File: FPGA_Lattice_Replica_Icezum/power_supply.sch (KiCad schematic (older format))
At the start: 53 parts, among them J18 Power_Jack, Q1 DMP3017, Q2 DMP3017, Q3 DMP2035U-7, Q4 Mosfet_P_DFN-6, Q5 PMBT3906, SW3 SPDT_Switch, SW4 Switch, U10 AP7361, U11 TLV711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

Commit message: se finalizo asignación de footprint de acuerdo al modelo original de la icezum alhambra
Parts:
- C59, C61: footprint (none) -> footprints:C_0603
- C63, C68: footprint (none) -> footprints:C_0402
- J18: footprint (none) -> footprints:JACK_2.1
- L4: footprint (none) -> footprints:L_0603
- L5: footprint (none) -> footprints:L_4040
- Q1, Q2, Q4: footprint (none) -> footprints:DFN-2523-6
- Q3, U13: footprint (none) -> footprints:SOT-23
- Q5: footprint Package_TO_SOT_SMD:SOT-363_SC-70-6 -> footprints:SOT-23
- R24, R25, R26, R27, R28, R29, R30, R33, R34, R35, R36, R37, R38, R39: footprint (none) -> footprints:R_0402
- SW3: footprint (none) -> footprints:slide-sw-spdt-right-angle
- SW4: footprint (none) -> footprints:SW_vert_tht_7.5x6x6.5
- TP1, TP2, TP3, TP4, TP5, TP6, TP7: footprint (none) -> footprints:Via_Test_point
- U10: footprint (none) -> footprints:DFN-3030-8
- U11: footprint (none) -> footprints:WSON-6
- U12: footprint (none) -> footprints:QFN16
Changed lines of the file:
@@
 F 0 "J18" H 3107 3925 50  0000 C CNN
 F 1 "Power_Jack" H 3107 3834 50  0000 C CNN
-F 2 "" H 3100 3560 50  0001 C CNN
+F 2 "footprints:JACK_2.1" H 3100 3560 50  0001 C CNN
 F 3 "~" H 3100 3560 50  0001 C CNN
 	1    3050 3600
@@
 F 0 "Q1" V 3702 3850 60  0000 C CNN
 F 1 "DMP3017" V 3808 3850 60  0000 C CNN
-F 2 "" H 4540 3830 60  0001 C CNN
+F 2 "footprints:DFN-2523-6" H 4540 3830 60  0001 C CNN
 F 3 "" H 4540 3830 60  0000 C CNN
 	1    4100 3500
@@
 F 0 "Q2" V 6102 3850 60  0000 C CNN
 F 1 "DMP3017" V 6208 3850 60  0000 C CNN
-F 2 "" H 6940 3830 60  0001 C CNN
+F 2 "footprints:DFN-2523-6" H 6940 3830 60  0001 C CNN
 F 3 "" H 6940 3830 60  0000 C CNN
 	1    6500 3500
@@
 F 0 "Q5" V 7385 4350 50  0000 C CNN
 F 1 "PMBT3906" V 7476 4350 50  0000 C CNN
-F 2 "Package_TO_SOT_SMD:SOT-363_SC-70-6" H 7350 4450 50  0001 C CNN
+F 2 "footprints:SOT-23" H 7350 4450 50  0001 C CNN
 F 3 "https://assets.nexperia.com/documents/data-sheet/PMBT3906YS.pdf" H 7150 4350 50  0001 C CNN
 	1    7150 4350
@@
 F 0 "Q3" V 7502 3975 60  0000 C CNN
 F 1 "DMP2035U-7" V 7608 3975 60  0000 C CNN
-F 2 "" H 8350 3950 60  0001 C CNN
+F 2 "footprints:SOT-23" H 8350 3950 60  0001 C CNN
 F 3 "" H 8350 3950 60  0000 C CNN
 	1    8350 3950
@@
 F 0 "C61" V 5302 3950 50  0000 C CNN
 F 1 "10 nF" V 5211 3950 50  0000 C CNN
-F 2 "" H 5088 3800 50  0001 C CNN
+F 2 "footprints:C_0603" H 5088 3800 50  0001 C CNN
 F 3 "~" H 5050 3950 50  0001 C CNN
 F 4 "X7R" V 5050 3950 50  0001 C CNN "Clase"
@@
 F 0 "R25" H 4620 4296 50  0000 L CNN
 F 1 "10K±5% 0.063 W" V 4450 3900 50  0000 L CNN
-F 2 "" V 4480 4250 50  0001 C CNN
+F 2 "footprints:R_0402" V 4480 4250 50  0001 C CNN
 F 3 "~" H 4550 4250 50  0001 C CNN
 	1    4550 4250
@@
 F 0 "R26" H 5420 4296 50  0000 L CNN
 F 1 "100K±5% 0.063 W" V 5250 3800 50  0000 L CNN
-F 2 "" V 5280 4250 50  0001 C CNN
+F 2 "footprints:R_0402" V 5280 4250 50  0001 C CNN
 F 3 "~" H 5350 4250 50  0001 C CNN
 	1    5350 4250
@@
 F 0 "R27" H 6120 4296 50  0000 L CNN
 F 1 "10K±5% 0.063 W" V 5950 3800 50  0000 L CNN
-F 2 "" V 5980 4250 50  0001 C CNN
+F 2 "footprints:R_0402" V 5980 4250 50  0001 C CNN
 F 3 "~" H 6050 4250 50  0001 C CNN
 	1    6050 4250
@@
 F 0 "R29" H 8270 4646 50  0000 L CNN
 F 1 "100K±5% 0.063 W" V 8100 4000 50  0000 L CNN
-F 2 "" V 8130 4600 50  0001 C CNN
+F 2 "footprints:R_0402" V 8130 4600 50  0001 C CNN
 F 3 "~" H 8200 4600 50  0001 C CNN
 	1    8200 4600
@@
 F 0 "R28" V 7593 4450 50  0000 C CNN
 F 1 "10K±5% 0.063 W" V 7684 4450 50  0000 C CNN
-F 2 "" V 7730 4450 50  0001 C CNN
+F 2 "footprints:R_0402" V 7730 4450 50  0001 C CNN
 F 3 "~" H 7800 4450 50  0001 C CNN
 	1    7800 4450
@@
 F 0 "R38" V 7450 3500 50  0000 C CNN
 F 1 "10K±5% 0.063 W" V 7250 3450 50  0000 C CNN
-F 2 "" V 7280 3500 50  0001 C CNN
+F 2 "footprints:R_0402" V 7280 3500 50  0001 C CNN
 F 3 "~" H 7350 3500 50  0001 C CNN
 	1    7350 3500
@@
 F 0 "R39" H 7870 3846 50  0000 L CNN
 F 1 "1K±5% 0.063 W" V 7700 3450 50  0000 L CNN
-F 2 "" V 7730 3800 50  0001 C CNN
+F 2 "footprints:R_0402" V 7730 3800 50  0001 C CNN
 F 3 "~" H 7800 3800 50  0001 C CNN
 	1    7800 3800
@@
 F 0 "TP6" H 6778 3442 60  0000 L CNN
 F 1 "TestPoint_Small" H 6700 3250 60  0001 C CNN
-F 2 "" H 6700 3350 60  0001 C CNN
+F 2 "footprints:Via_Test_point" H 6700 3350 60  0001 C CNN
 F 3 "" H 6700 3350 60  0000 C CNN
 	1    6700 3350
@@
 F 0 "SW3" H 7325 5441 47  0000 C CNN
 F 1 "SPDT_Switch" H 7325 5354 47  0000 C CNN
-F 2 "" H 6950 5100 60  0001 C CNN
+F 2 "footprints:slide-sw-spdt-right-angle" H 6950 5100 60  0001 C CNN
 F 3 "" H 6950 5100 60  0000 C CNN
 	1    6950 5100
@@
 F 0 "R24" V 6300 3950 50  0000 C CNN
 F 1 "10K±5% 0.063 W" V 6500 3950 50  0000 C CNN
-F 2 "" V 6330 3950 50  0001 C CNN
+F 2 "footprints:R_0402" V 6330 3950 50  0001 C CNN
 F 3 "~" H 6400 3950 50  0001 C CNN
 	1    6400 3950
@@
 F 0 "TP7" H 7878 3386 60  0000 L CNN
 F 1 "TestPoint_Small" H 7800 3250 60  0001 C CNN
-F 2 "" H 7800 3350 60  0001 C CNN
+F 2 "footprints:Via_Test_point" H 7800 3350 60  0001 C CNN
 F 3 "" H 7800 3350 60  0000 C CNN
 	1    7800 3350
@@
 F 0 "U12" H 2650 6099 60  0000 C CNN
 F 1 "TPS62133RGTR" H 2650 5993 60  0000 C CNN
-F 2 "" H 2210 5910 60  0001 C CNN
+F 2 "footprints:QFN16" H 2210 5910 60  0001 C CNN
 F 3 "" H 2210 5910 60  0000 C CNN
 	1    2100 5800
@@
 F 0 "L4" H 1075 6244 60  0000 C CNN
 F 1 "Ferrite_Bead" H 780 5890 60  0001 L BNN
-F 2 "" H 750 6000 60  0001 C CNN
+F 2 "footprints:L_0603" H 750 6000 60  0001 C CNN
 F 3 "" H 750 6000 60  0000 C CNN
 F 4 "BLM18SG121TN1D" H 1075 6138 60  0000 C CNN "OrderingCode"
@@
 F 0 "C68" H 4150 6450 50  0000 L CNN
 F 1 "100 nF" H 4150 6250 50  0000 L CNN
-F 2 "" H 4138 6200 50  0001 C CNN
+F 2 "footprints:C_0402" H 4138 6200 50  0001 C CNN
 F 3 "~" H 4100 6350 50  0001 C CNN
 	1    4100 6350
@@
 F 0 "L5" H 3750 6394 60  0000 C CNN
 F 1 "2.2 uH 4,7A" H 3750 6288 60  0000 C CNN
-F 2 "" H 3400 6150 60  0001 C CNN
+F 2 "footprints:L_4040" H 3400 6150 60  0001 C CNN
 F 3 "" H 3400 6150 60  0000 C CNN
 	1    3400 6150
@@
 F 0 "C63" H 6565 6746 50  0000 L CNN
 F 1 "100 nF" H 6565 6655 50  0000 L CNN
-F 2 "" H 6488 6550 50  0001 C CNN
+F 2 "footprints:C_0402" H 6488 6550 50  0001 C CNN
 F 3 "~" H 6450 6700 50  0001 C CNN
 	1    6450 6700
@@
 F 0 "R33" V 5100 7400 50  0000 C CNN
 F 1 "10K±5% 0.063 W" V 5200 7400 50  0000 C CNN
-F 2 "" V 5230 7350 50  0001 C CNN
+F 2 "footprints:R_0402" V 5230 7350 50  0001 C CNN
 F 3 "~" H 5300 7350 50  0001 C CNN
 	1    5300 7350
@@
 F 0 "R35" V 5900 7350 50  0000 C CNN
 F 1 "100K±5% 0.063 W" V 6000 7300 50  0000 C CNN
-F 2 "" V 6030 7350 50  0001 C CNN
+F 2 "footprints:R_0402" V 6030 7350 50  0001 C CNN
 F 3 "~" H 6100 7350 50  0001 C CNN
 	1    6100 7350
@@
 F 0 "U13" H 4083 7787 60  0000 C CNN
 F 1 "APX810" H 4083 7681 60  0000 C CNN
-F 2 "" H 3700 7650 157 0001 C CNN
+F 2 "footprints:SOT-23" H 3700 7650 157 0001 C CNN
 F 3 "" H 4000 7350 157 0001 C CNN
 	1    4000 7350
@@
 F 0 "R36" H 4900 6700 50  0000 L CNN
 F 1 "100K±5% 0.063 W" V 5100 6200 50  0000 L CNN
-F 2 "" V 4830 6550 50  0001 C CNN
+F 2 "footprints:R_0402" V 4830 6550 50  0001 C CNN
 F 3 "~" H 4900 6550 50  0001 C CNN
 	1    4900 6550
@@
 F 0 "TP5" H 6878 5892 60  0000 L CNN
 F 1 "TestPoint_Small" H 6800 5700 60  0001 C CNN
-F 2 "" H 6800 5800 60  0001 C CNN
+F 2 "footprints:Via_Test_point" H 6800 5800 60  0001 C CNN
 F 3 "" H 6800 5800 60  0000 C CNN
 	1    6800 5800
@@
 F 0 "TP1" H 4828 5892 60  0000 L CNN
 F 1 "TestPoint_Small" H 4750 5700 60  0001 C CNN
-F 2 "" H 4750 5800 60  0001 C CNN
+F 2 "footprints:Via_Test_point" H 4750 5800 60  0001 C CNN
 F 3 "" H 4750 5800 60  0000 C CNN
 	1    4750 5800
@@
 F 0 "R37" H 4970 7646 50  0000 L CNN
 F 1 "10K±5% 0.063 W" H 4970 7555 50  0000 L CNN
-F 2 "" V 4830 7600 50  0001 C CNN
+F 2 "footprints:R_0402" V 4830 7600 50  0001 C CNN
 F 3 "~" H 4900 7600 50  0001 C CNN
 	1    4900 7600
@@
 F 0 "Q4" V 5752 6500 60  0000 C CNN
 F 1 "Mosfet_P_DFN-6" V 5858 6500 60  0000 C CNN
-F 2 "" H 6590 6480 60  0001 C CNN
+F 2 "footprints:DFN-2523-6" H 6590 6480 60  0001 C CNN
 F 3 "" H 6590 6480 60  0000 C CNN
 	1    6150 6150
@@
 F 0 "SW4" H 9000 6250 60  0000 C CNN
 F 1 "Switch" H 9000 5950 60  0000 C CNN
-F 2 "" H 8600 6050 60  0001 C CNN
+F 2 "footprints:SW_vert_tht_7.5x6x6.5" H 8600 6050 60  0001 C CNN
 F 3 "" H 8600 6050 60  0000 C CNN
 	1    8600 6050
@@
 F 0 "R30" H 9520 5396 50  0000 L CNN
 F 1 "10K±5% 0.063 W" V 9350 5000 50  0000 L CNN
-F 2 "" V 9380 5350 50  0001 C CNN
+F 2 "footprints:R_0402" V 9380 5350 50  0001 C CNN
 F 3 "~" H 9450 5350 50  0001 C CNN
 	1    9450 5350
@@
 F 0 "R34" H 870 3696 50  0000 L CNN
 F 1 "10K±5% 0.063 W" H 870 3605 50  0000 L CNN
-F 2 "" V 730 3650 50  0001 C CNN
+F 2 "footprints:R_0402" V 730 3650 50  0001 C CNN
 F 3 "~" H 800 3650 50  0001 C CNN
 	1    800  3650
@@
 F 0 "U10" H 3100 1899 60  0000 C CNN
 F 1 "AP7361" H 3100 1793 60  0000 C CNN
-F 2 "" H 2670 1710 60  0001 C CNN
+F 2 "footprints:DFN-3030-8" H 2670 1710 60  0001 C CNN
 F 3 "" H 2670 1710 60  0000 C CNN
 	1    2450 1600
@@
 F 0 "C59" H 3065 1796 50  0000 L CNN
 F 1 "4.7 uF" H 3065 1705 50  0000 L CNN
-F 2 "" H 2988 1600 50  0001 C CNN
+F 2 "footprints:C_0603" H 2988 1600 50  0001 C CNN
 F 3 "~" H 2950 1750 50  0001 C CNN
 	1    2950 1750
@@
 F 0 "TP2" H 3428 1242 60  0000 L CNN
 F 1 "TestPoint_Small" H 3350 1050 60  0001 C CNN
-F 2 "" H 3350 1150 60  0001 C CNN
+F 2 "footprints:Via_Test_point" H 3350 1150 60  0001 C CNN
 F 3 "" H 3350 1150 60  0000 C CNN
 	1    3350 1150
@@
 F 0 "TP3" H 7528 1642 60  0000 L CNN
 F 1 "TestPoint_Small" H 7450 1450 60  0001 C CNN
-F 2 "" H 7450 1550 60  0001 C CNN
+F 2 "footprints:Via_Test_point" H 7450 1550 60  0001 C CNN
 F 3 "" H 7450 1550 60  0000 C CNN
 	1    7450 1550
@@
 F 0 "TP4" H 6828 1642 60  0000 L CNN
 F 1 "TestPoint_Small" H 6750 1450 60  0001 C CNN
-F 2 "" H 6750 1550 60  0001 C CNN
+F 2 "footprints:Via_Test_point" H 6750 1550 60  0001 C CNN
 F 3 "" H 6750 1550 60  0000 C CNN
 	1    6750 1550
@@
 F 0 "U11" H 5350 1899 60  0000 C CNN
 F 1 "TLV711" H 5350 1793 60  0000 C CNN
-F 2 "" H 4970 1710 60  0001 C CNN
+F 2 "footprints:WSON-6" H 4970 1710 60  0001 C CNN
 F 3 "" H 4970 1710 60  0000 C CNN
 	1    4750 1600

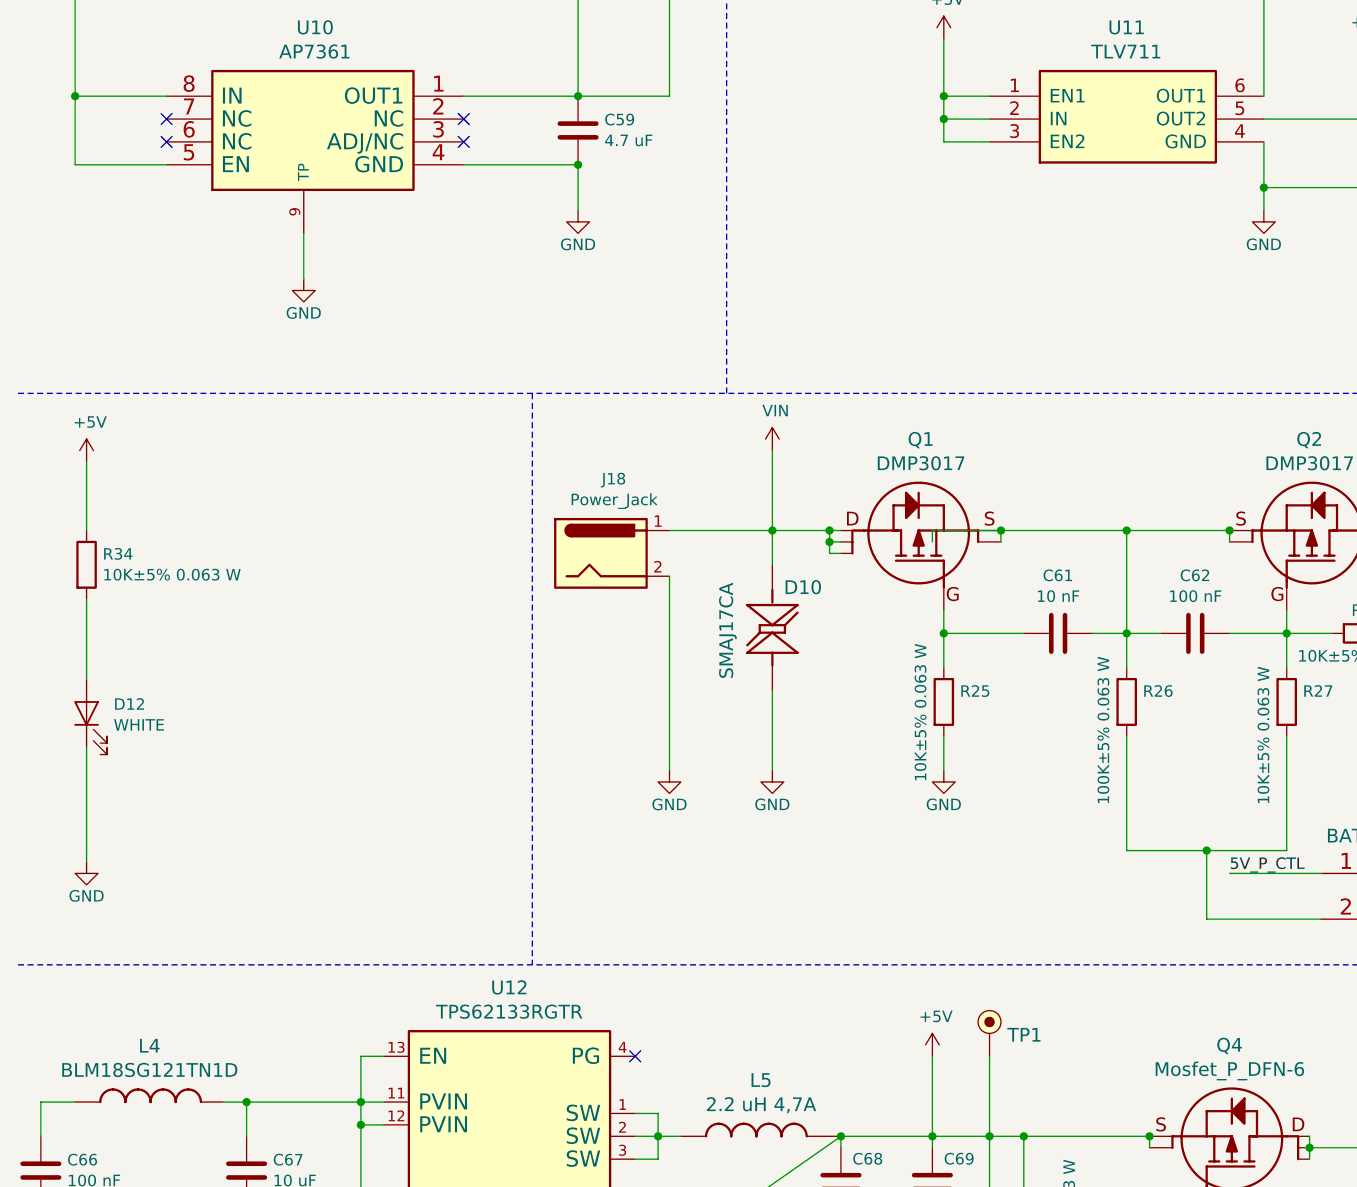
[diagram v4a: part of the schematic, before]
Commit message: se coloco hojas de datos de los componentes
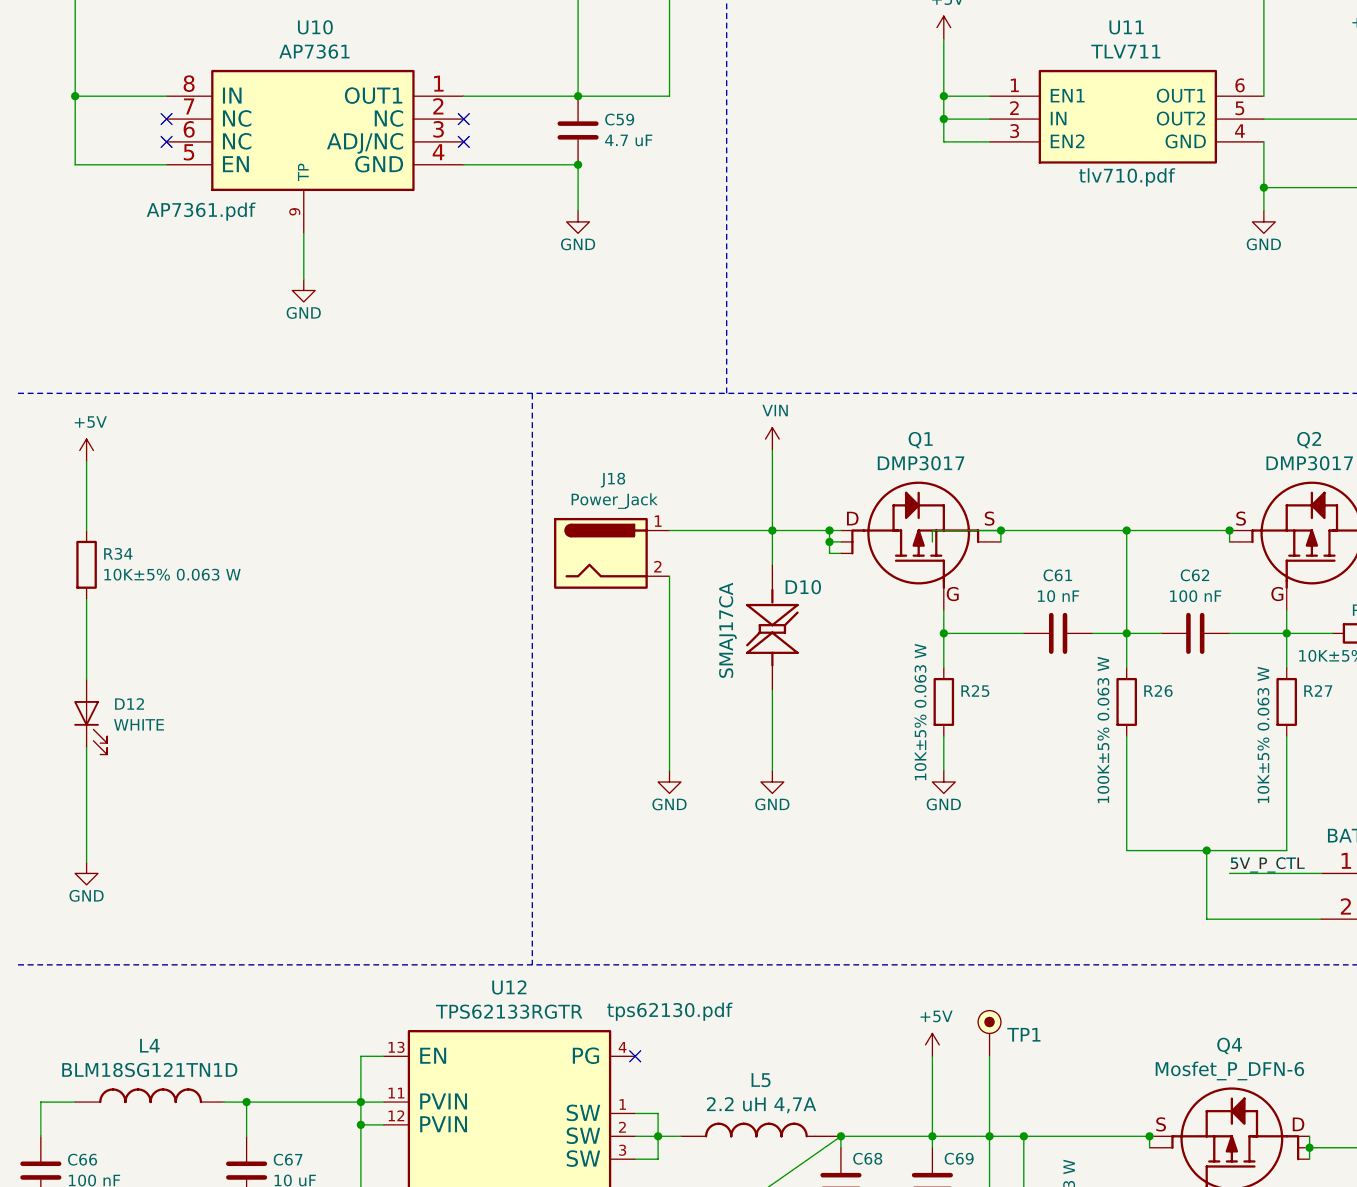
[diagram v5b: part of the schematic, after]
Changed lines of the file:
@@
 F 1 "TPS62133RGTR" H 2650 5993 60  0000 C CNN
 F 2 "footprints:QFN16" H 2210 5910 60  0001 C CNN
-F 3 "" H 2210 5910 60  0000 C CNN
+F 3 "tps62130.pdf" H 3350 6000 60  0000 C CNN
 	1    2100 5800
 	1    0    0    -1
@@
 F 1 "AP7361" H 3100 1793 60  0000 C CNN
 F 2 "footprints:DFN-3030-8" H 2670 1710 60  0001 C CNN
-F 3 "" H 2670 1710 60  0000 C CNN
+F 3 "AP7361.pdf" H 3600 1100 60  0000 C CNN
 	1    2450 1600
 	-1   0    0    -1
@@
 F 1 "TLV711" H 5350 1793 60  0000 C CNN
 F 2 "footprints:WSON-6" H 4970 1710 60  0001 C CNN
-F 3 "" H 4970 1710 60  0000 C CNN
+F 3 "tlv710.pdf" H 5350 1250 60  0000 C CNN
 	1    4750 1600
 	1    0    0    -1

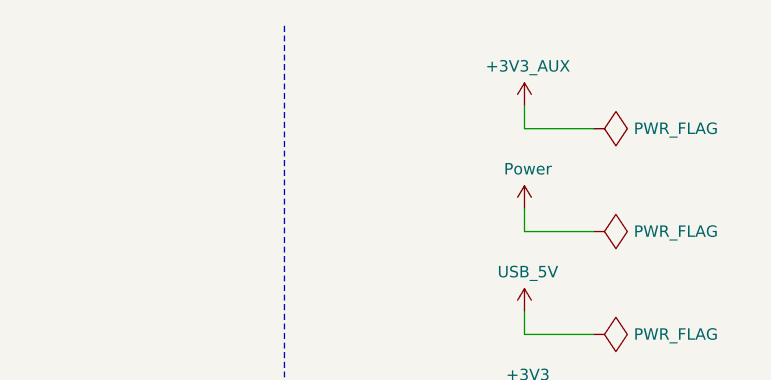
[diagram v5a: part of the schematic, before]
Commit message: se realizo las correcciones sugeridas por el revisor
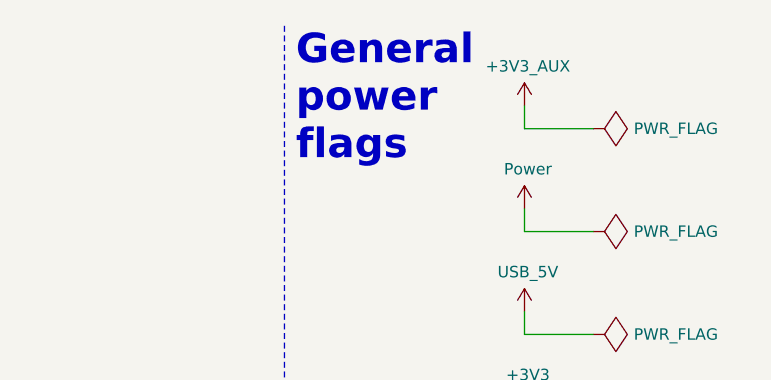
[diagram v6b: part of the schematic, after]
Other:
- note added: "General \npower \nflags"
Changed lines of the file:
@@
 	4750 6850 4750 6150
 NoConn ~ 3200 5800
+Text Notes 9200 1100 0    129  ~ 26
+General \npower \nflags
 $EndSCHEMATC
